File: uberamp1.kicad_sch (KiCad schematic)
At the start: 8 parts

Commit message: board outline
+ fix voltage range label
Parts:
- added H2, H3, H4, H5: ~, MountingHole:MountingHole_3.2mm_M3_DIN965_Pad_TopBottom, symbol Mechanical:MountingHole_Pad
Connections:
- new net GND: H2.1, H3.1, H4.1, H5.1

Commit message: final touches. Sent for production.
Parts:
- added s45: ref, invendelirium_general:pad_1.2x1.5, symbol Connector:TestPoint
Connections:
- net inputref: now also s45.1
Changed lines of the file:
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@@
 	)
 	(junction
+		(at 226.06 92.71)
+		(diameter 0)
+		(color 0 0 0 0)
+	)
+	(junction
 		(at 44.45 137.16)
 		(diameter 0)
@@
 	(wire
 		(pts
-			(xy 227.33 92.71) (xy 214.63 92.71)
+			(xy 227.33 92.71) (xy 226.06 92.71)
 		)
 		(stroke
@@
 	(wire
 		(pts
+			(xy 226.06 92.71) (xy 214.63 92.71)
+		)
+		(stroke
+			(width 0)
+			(type default)
+		)
+	)
+	(wire
+		(pts
 			(xy 88.9 127) (xy 129.54 127)
 		)
@@
 					(unit 1)
 				)
+			)
+		)
+	)
+	(symbol
+		(lib_id "Connector:TestPoint")
+		(at 226.06 92.71 0)
+		(unit 1)
+		(exclude_from_sim no)
+		(in_bom yes)
+		(on_board yes)
+		(dnp no)
+		(property "Reference" "s45"
+			(at 224.79 86.36 0)
+			(effects
+				(font
+					(size 1.27 1.27)
+				)
+				(justify left)
+			)
+		)
+		(property "Value" "ref"
+			(at 224.79 87.63 0)
+			(effects
+				(font
+					(size 1.27 1.27)
+				)
+				(justify left)
+			)
+		)
+		(property "Footprint" "invendelirium_general:pad_1.2x1.5"
+			(at 231.14 92.71 0)
+			(effects
+				(font
+					(size 1.27 1.27)
+				)
+				(hide yes)
+			)
+		)
+		(property "Datasheet" "~"
+			(at 231.14 92.71 0)
+			(effects
+				(font
+					(size 1.27 1.27)
+				)
+				(hide yes)
+			)
+		)
+		(property "Description" ""
+			(at 226.06 92.71 0)
+			(effects
+				(font
+					(size 1.27 1.27)
+				)
+				(hide yes)
+			)
+		)
+		(property "Sim.Device" ""
+			(at 226.06 92.71 0)
+			(effects
+				(font
+					(size 1.27 1.27)
+				)
+				(hide yes)
+			)
+		)
+		(property "Sim.Library" ""
+			(at 226.06 92.71 0)
+			(effects
+				(font
+					(size 1.27 1.27)
+				)
+				(hide yes)
+			)
+		)
+		(property "Sim.Name" ""
+			(at 226.06 92.71 0)
+			(effects
+				(font
+					(size 1.27 1.27)
+				)
+				(hide yes)
+			)
+		)
+		(property "Sim.Pins" ""
+			(at 226.06 92.71 0)
+			(effects
+				(font
+					(size 1.27 1.27)
+				)
+				(hide yes)
+			)
+		)
+		(pin "1"
+		)
+		(instances
+			(project "uberamp1"
+				(path "/310059c1-d84b-43e2-9c9a-0e426c534a12"
+					(reference "s45")
+					(unit 1)
+				)

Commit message: work on bugs...
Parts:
- added H6: heatsink hole, MountingHole:MountingHole_2.2mm_M2_DIN965_Pad, symbol Mechanical:MountingHole_Pad
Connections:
- net GND: now also H6.1
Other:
- sheet dac0 ports: added pg; removed none
- sheet dac1 ports: added pg; removed none
- sheet poweramp ports: added c_start; removed none
- sheet poweramp1 ports: added c_start; removed none
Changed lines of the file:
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@@
 	)
 	(junction
+		(at 107.95 191.77)
+		(diameter 0)
+		(color 0 0 0 0)
+	)
+	(junction
 		(at 191.77 73.66)
 		(diameter 0)
@@
 	(wire
 		(pts
+			(xy 251.46 146.05) (xy 252.73 146.05)
+		)
+		(stroke
+			(width 0)
+			(type default)
+		)
+	)
+	(wire
+		(pts
 			(xy 135.89 97.79) (xy 133.35 97.79)
 		)
@@
 	(wire
 		(pts
+			(xy 251.46 92.71) (xy 251.46 91.44)
+		)
+		(stroke
+			(width 0)
+			(type default)
+		)
+	)
+	(wire
+		(pts
 			(xy 151.13 85.09) (xy 151.13 82.55)
 		)
@@
 	(wire
 		(pts
+			(xy 251.46 142.24) (xy 251.46 146.05)
+		)
+		(stroke
+			(width 0)
+			(type default)
+		)
+	)
+	(wire
+		(pts
 			(xy 209.55 127) (xy 209.55 161.29)
 		)
@@
 	(wire
 		(pts
+			(xy 142.24 106.68) (xy 142.24 110.49)
+		)
+		(stroke
+			(width 0)
+			(type default)
+		)
+	)
+	(wire
+		(pts
 			(xy 132.08 93.98) (xy 135.89 93.98)
 		)
@@
 	(wire
 		(pts
+			(xy 138.43 106.68) (xy 142.24 106.68)
+		)
+		(stroke
+			(width 0)
+			(type default)
+		)
+	)
+	(wire
+		(pts
 			(xy 189.23 54.61) (xy 165.1 54.61)
 		)
@@
 	(wire
 		(pts
+			(xy 252.73 92.71) (xy 251.46 92.71)
+		)
+		(stroke
+			(width 0)
+			(type default)
+		)
+	)
+	(wire
+		(pts
 			(xy 212.09 125.73) (xy 214.63 125.73)
 		)
@@
 	(wire
 		(pts
+			(xy 252.73 146.05) (xy 252.73 92.71)
+		)
+		(stroke
+			(width 0)
+			(type default)
+		)
+	)
+	(wire
+		(pts
+			(xy 107.95 191.77) (xy 116.84 191.77)
+		)
+		(stroke
+			(width 0)
+			(type default)
+		)
+	)
+	(wire
+		(pts
 			(xy 254 146.05) (xy 254 95.25)
 		)
@@
 	(wire
 		(pts
+			(xy 142.24 81.28) (xy 142.24 85.09)
+		)
+		(stroke
+			(width 0)
+			(type default)
+		)
+	)
+	(wire
+		(pts
 			(xy 88.9 127) (xy 129.54 127)
 		)
@@
 	(wire
 		(pts
+			(xy 138.43 81.28) (xy 142.24 81.28)
+		)
+		(stroke
+			(width 0)
+			(type default)
+		)
+	)
+	(wire
+		(pts
 			(xy 180.34 125.73) (xy 180.34 133.35)
 		)
@@
 		)
 	)
+	(label "pg"
+		(at 139.7 106.68 0)
+		(fields_autoplaced yes)
+		(effects
+			(font
+				(size 1.016 1.016)
+			)
+			(justify left bottom)
+		)
+	)
 	(label "12V"
 		(at 171.45 175.26 180)
@@
 		)
 	)
+	(label "pg"
+		(at 139.7 81.28 0)
+		(fields_autoplaced yes)
+		(effects
+			(font
+				(size 1.016 1.016)
+			)
+			(justify left bottom)
+		)
+	)
 	(label "12V"
 		(at 254 52.07 180)
@@
 	)
 	(symbol
+		(lib_id "Mechanical:MountingHole_Pad")
+		(at 116.84 189.23 0)
+		(unit 1)
+		(exclude_from_sim yes)
+		(in_bom no)
+		(on_board yes)
+		(dnp no)
+		(fields_autoplaced yes)
+		(property "Reference" "H6"
+			(at 119.38 186.6899 0)
+			(effects
+				(font
+					(size 1.27 1.27)
+				)
+				(justify left)
+			)
+		)
+		(property "Value" "heatsink hole"
+			(at 119.38 189.2299 0)
+			(effects
+				(font
+					(size 1.27 1.27)
+				)
+				(justify left)
+			)
+		)
+		(property "Footprint" "MountingHole:MountingHole_2.2mm_M2_DIN965_Pad"
+			(at 116.84 189.23 0)
+			(effects
+				(font
+					(size 1.27 1.27)
+				)
+				(hide yes)
+			)
+		)
+		(property "Datasheet" "~"
+			(at 116.84 189.23 0)
+			(effects
+				(font
+					(size 1.27 1.27)
+				)
+				(hide yes)
+			)
+		)
+		(property "Description" "Mounting Hole with connection"
+			(at 116.84 189.23 0)
+			(effects
+				(font
+					(size 1.27 1.27)
+				)
+				(hide yes)
+			)
+		)
+		(pin "1"
+		)
+		(instances
+			(project "uberamp1"
+				(path "/310059c1-d84b-43e2-9c9a-0e426c534a12"
+					(reference "H6")
+					(unit 1)
+				)
+			)
+		)
+	)
+	(symbol
 		(lib_id "power:+5V")
 		(at 99.06 85.09 0)
@@
 			)
 		)
+		(pin "c_start" passive
+			(at 251.46 91.44 270)
+			(effects
+				(font
+					(size 1.016 1.016)
+				)
+				(justify left)
+			)
+		)
 		(instances
 			(project "uberamp1"
@@
 			)
 		)
+		(pin "pg" input
+			(at 142.24 110.49 90)
+			(effects
+				(font
+					(size 1.016 1.016)
+				)
+				(justify right)
+			)
+		)
 		(instances
 			(project "uberamp1"
@@
 			)
 		)
+		(pin "pg" input
+			(at 142.24 85.09 90)
+			(effects
+				(font
+					(size 1.016 1.016)
+				)
+				(justify right)
+			)
+		)
 		(instances
 			(project "uberamp1"
@@
 			)
 		)
+		(pin "c_start" passive
+			(at 251.46 142.24 270)
+			(effects
+				(font
+					(size 1.016 1.016)
+				)
+				(justify left)
+			)
+		)

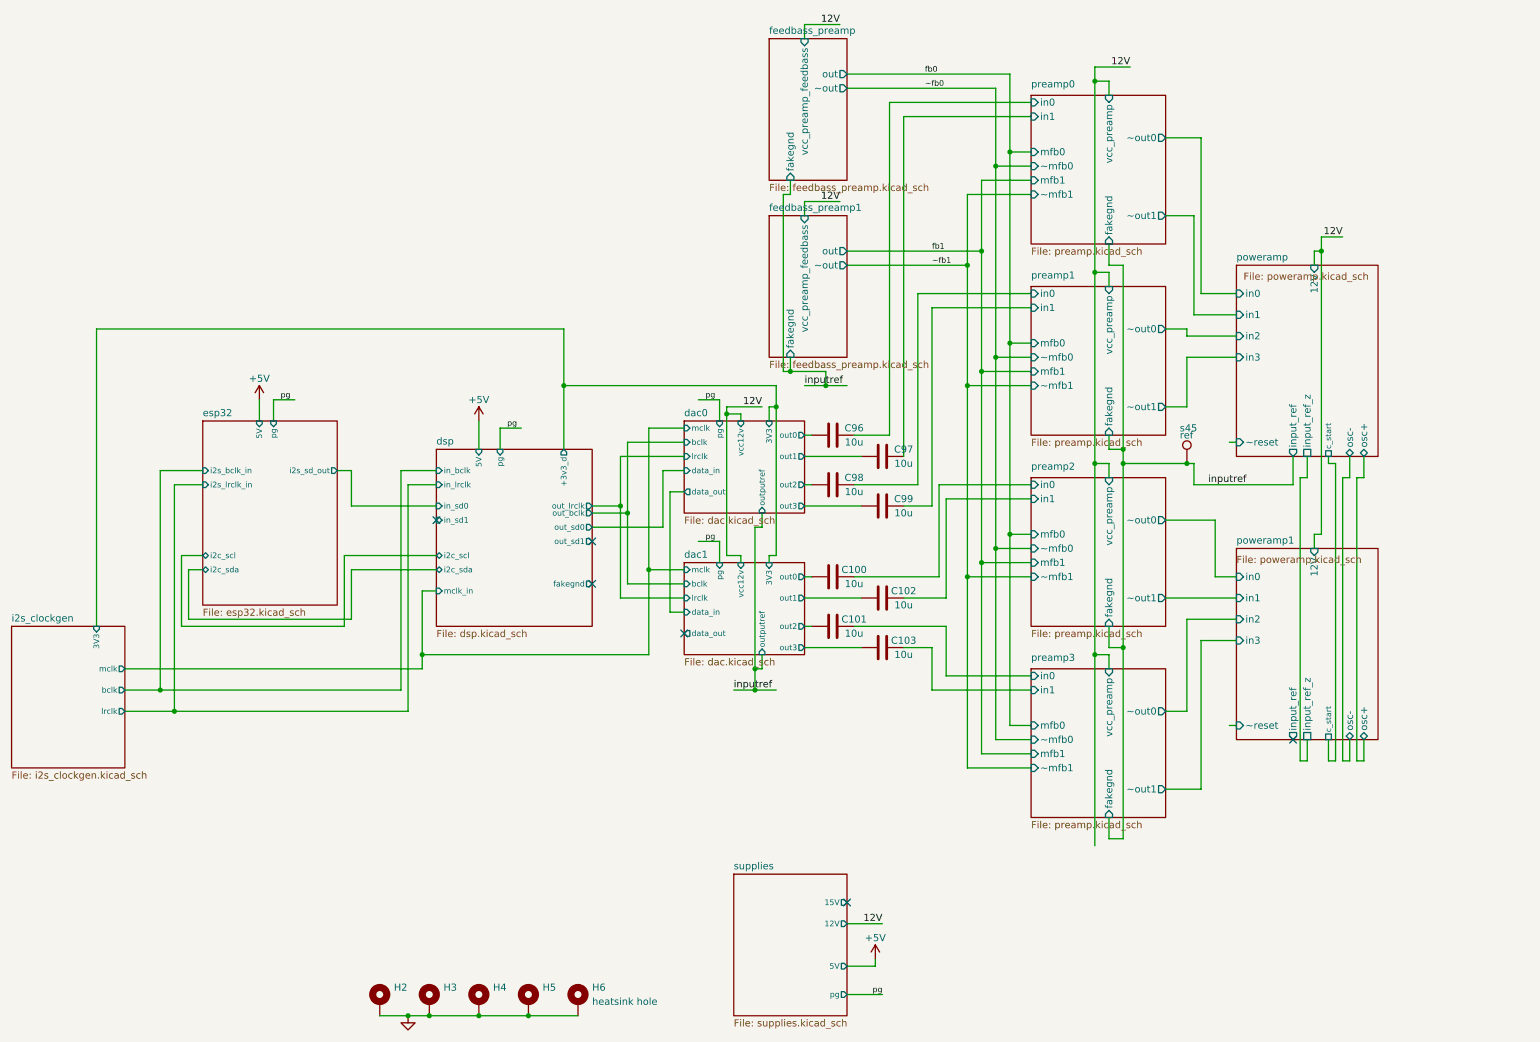
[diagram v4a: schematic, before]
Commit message: work on bugs
* align parts
* enlarge cercaps
* fix ak caps
* improve jack footprint
* fix lmr stencil openings
* remove one ldo
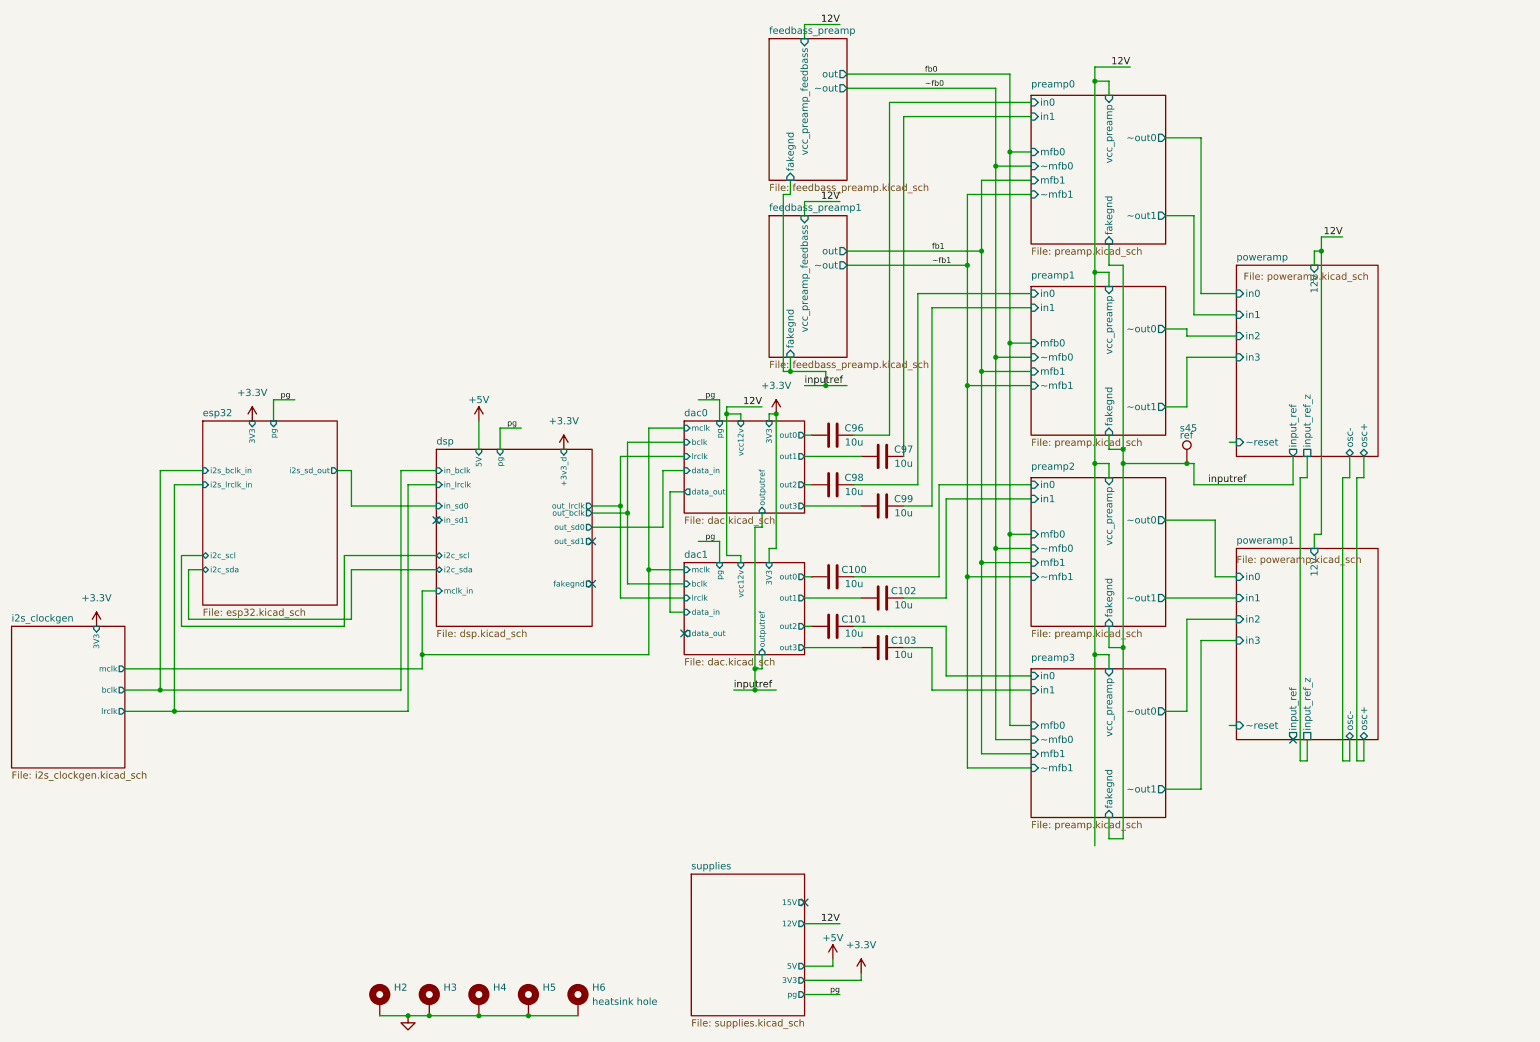
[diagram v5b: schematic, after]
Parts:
- C100, C101, C102, C103, C96, C97, C98, C99: footprint invendelirium_audio:C_0603 -> invendelirium_audio:C_0603_larger
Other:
- sheet esp32 ports: added 3V3; removed 5V
- sheet poweramp ports: added none; removed c_start
- sheet poweramp1 ports: added none; removed c_start
- sheet supplies ports: added 3V3; removed none

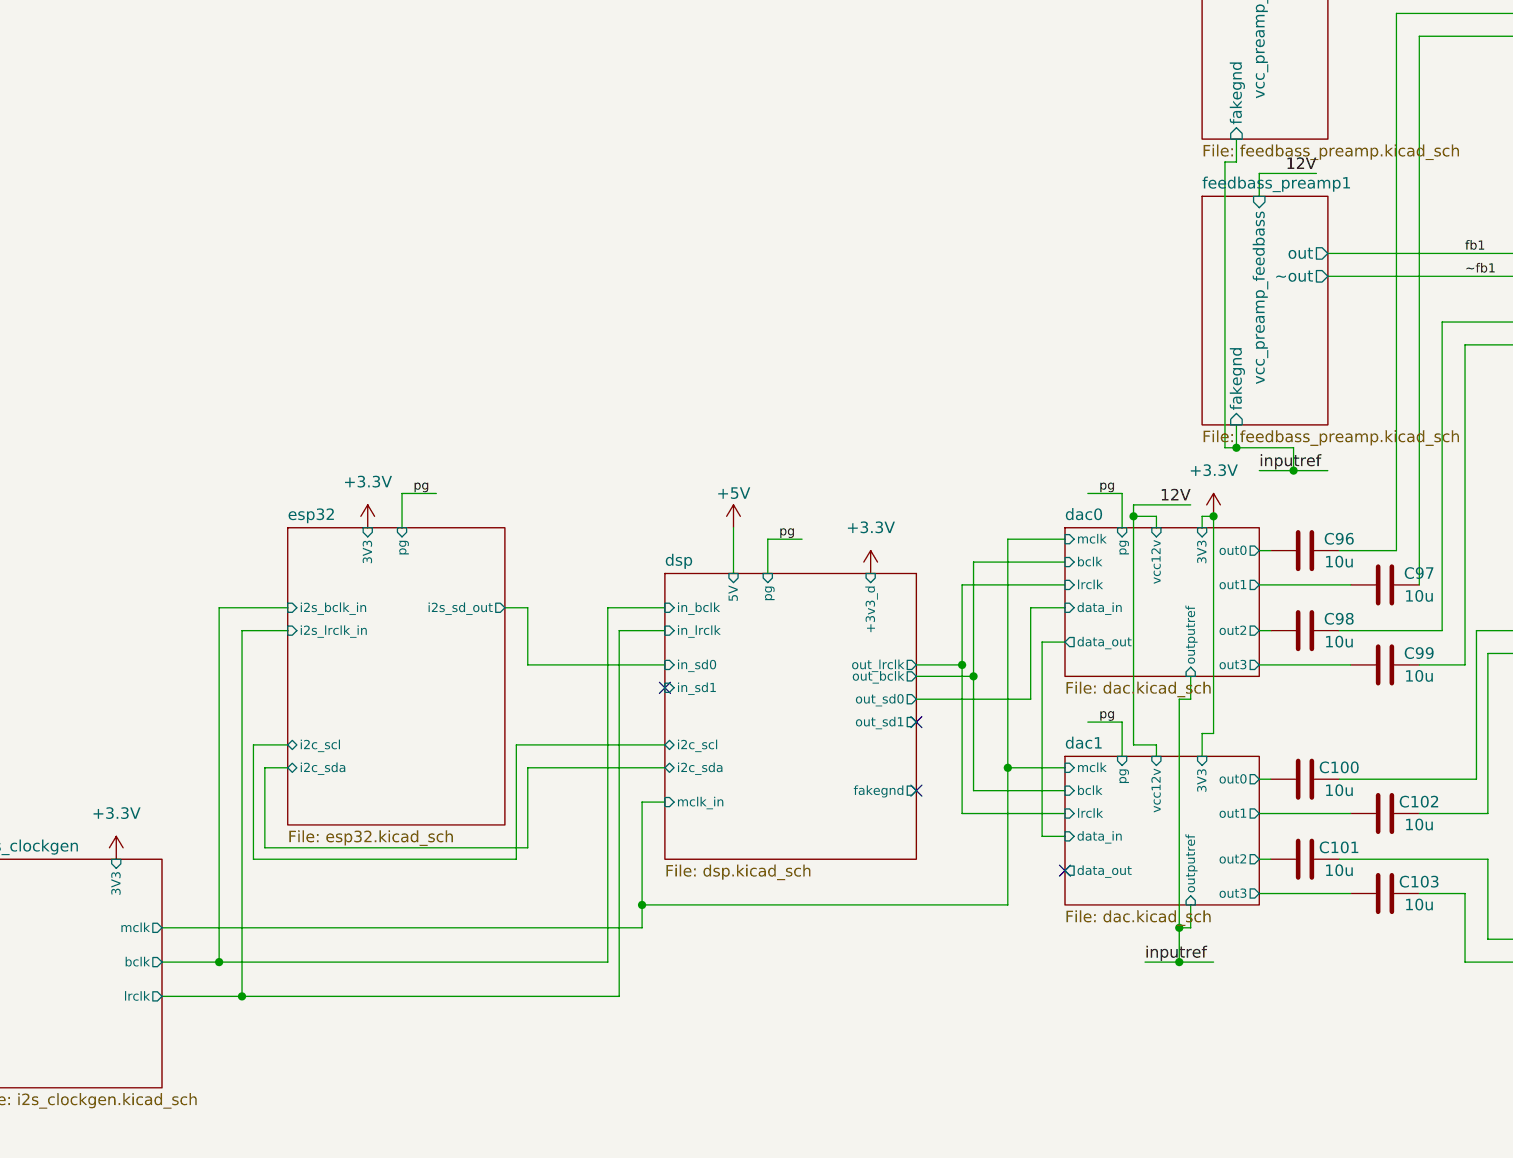
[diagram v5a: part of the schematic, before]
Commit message: remove duplicate dac supply
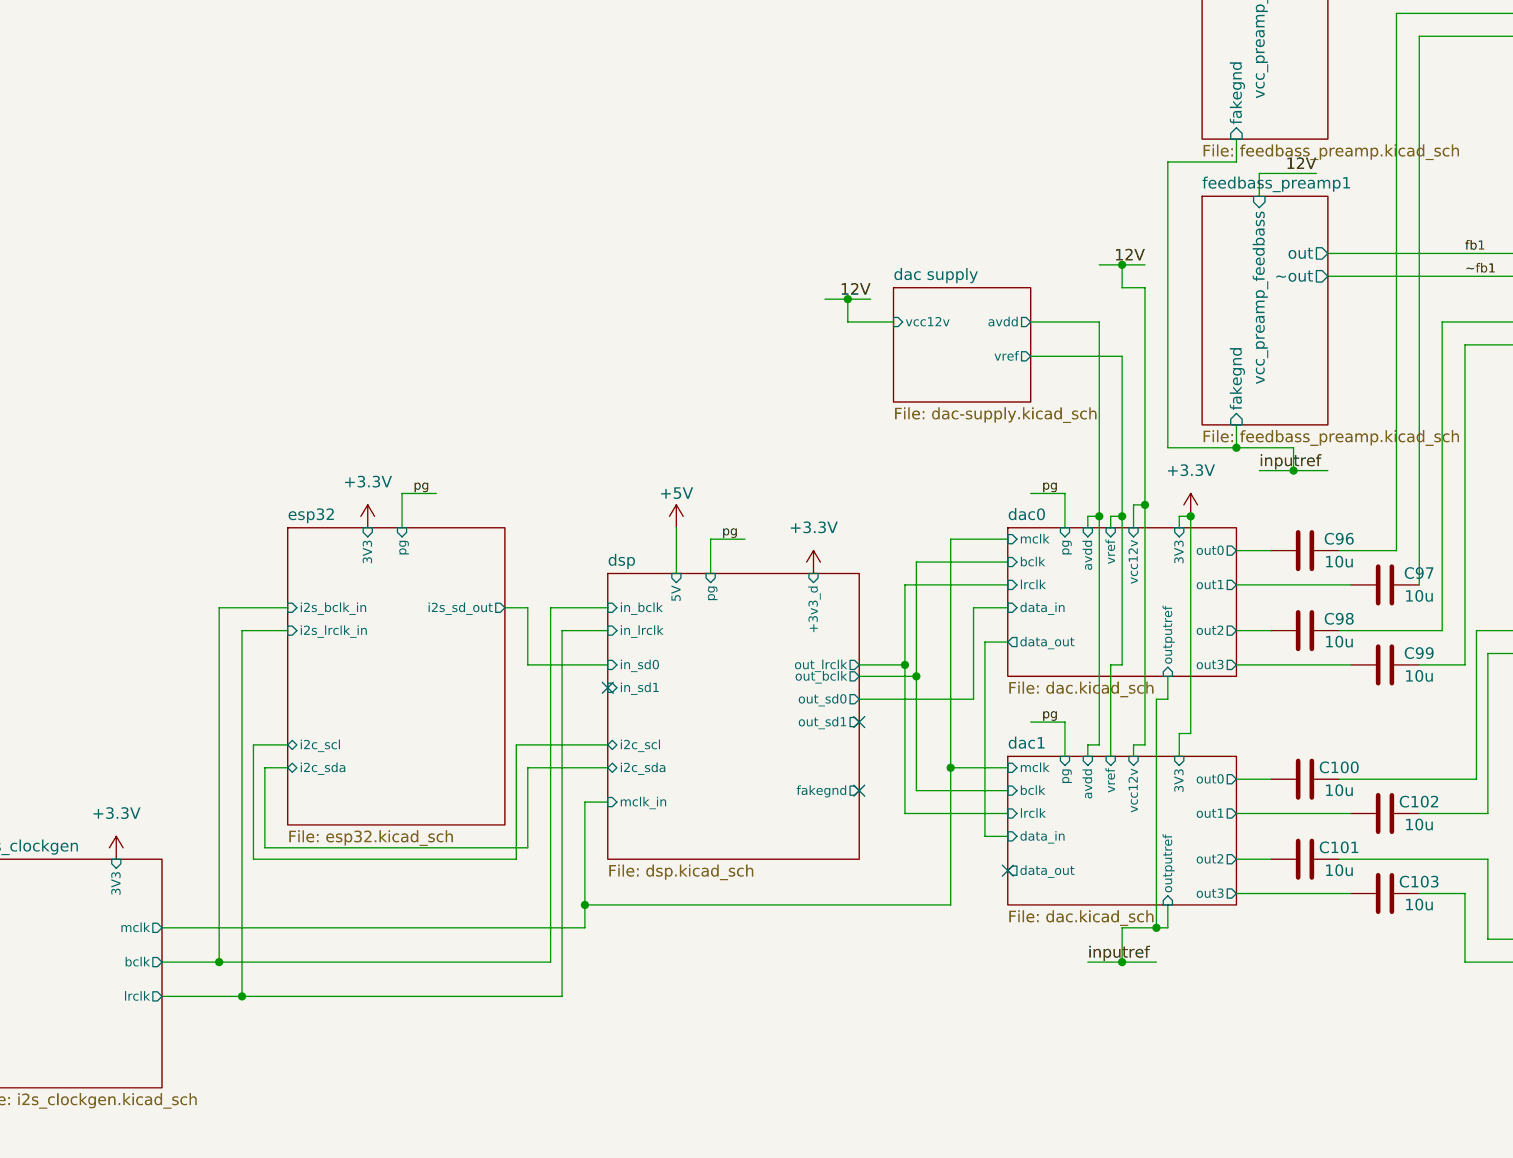
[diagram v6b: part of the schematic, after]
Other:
- added sheet dac supply (dac-supply.kicad_sch)
- sheet dac0 ports: added avdd, vref; removed none
- sheet dac1 ports: added avdd, vref; removed none
